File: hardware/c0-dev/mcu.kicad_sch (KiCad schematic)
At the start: 28 parts, among them J2 TAG_CONNECT, U11 W25Q128JVP, U12 RP2350A, Y1 ABM8-272-T3 (12Mhz)

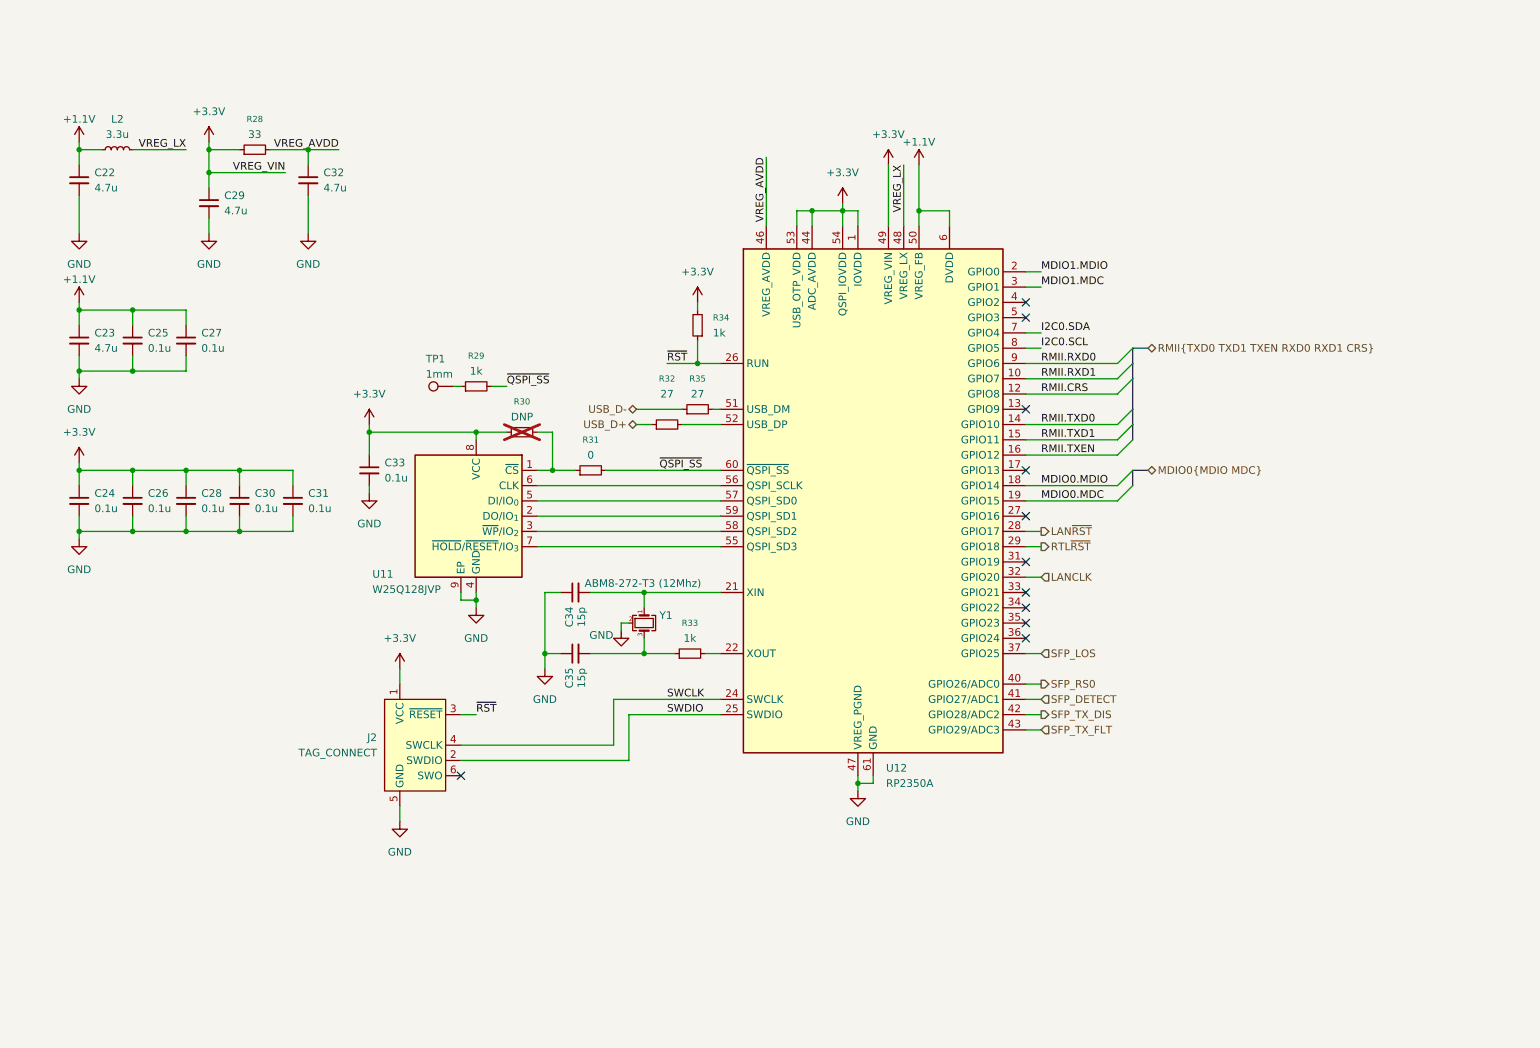
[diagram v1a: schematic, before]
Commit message: added 420 inputs
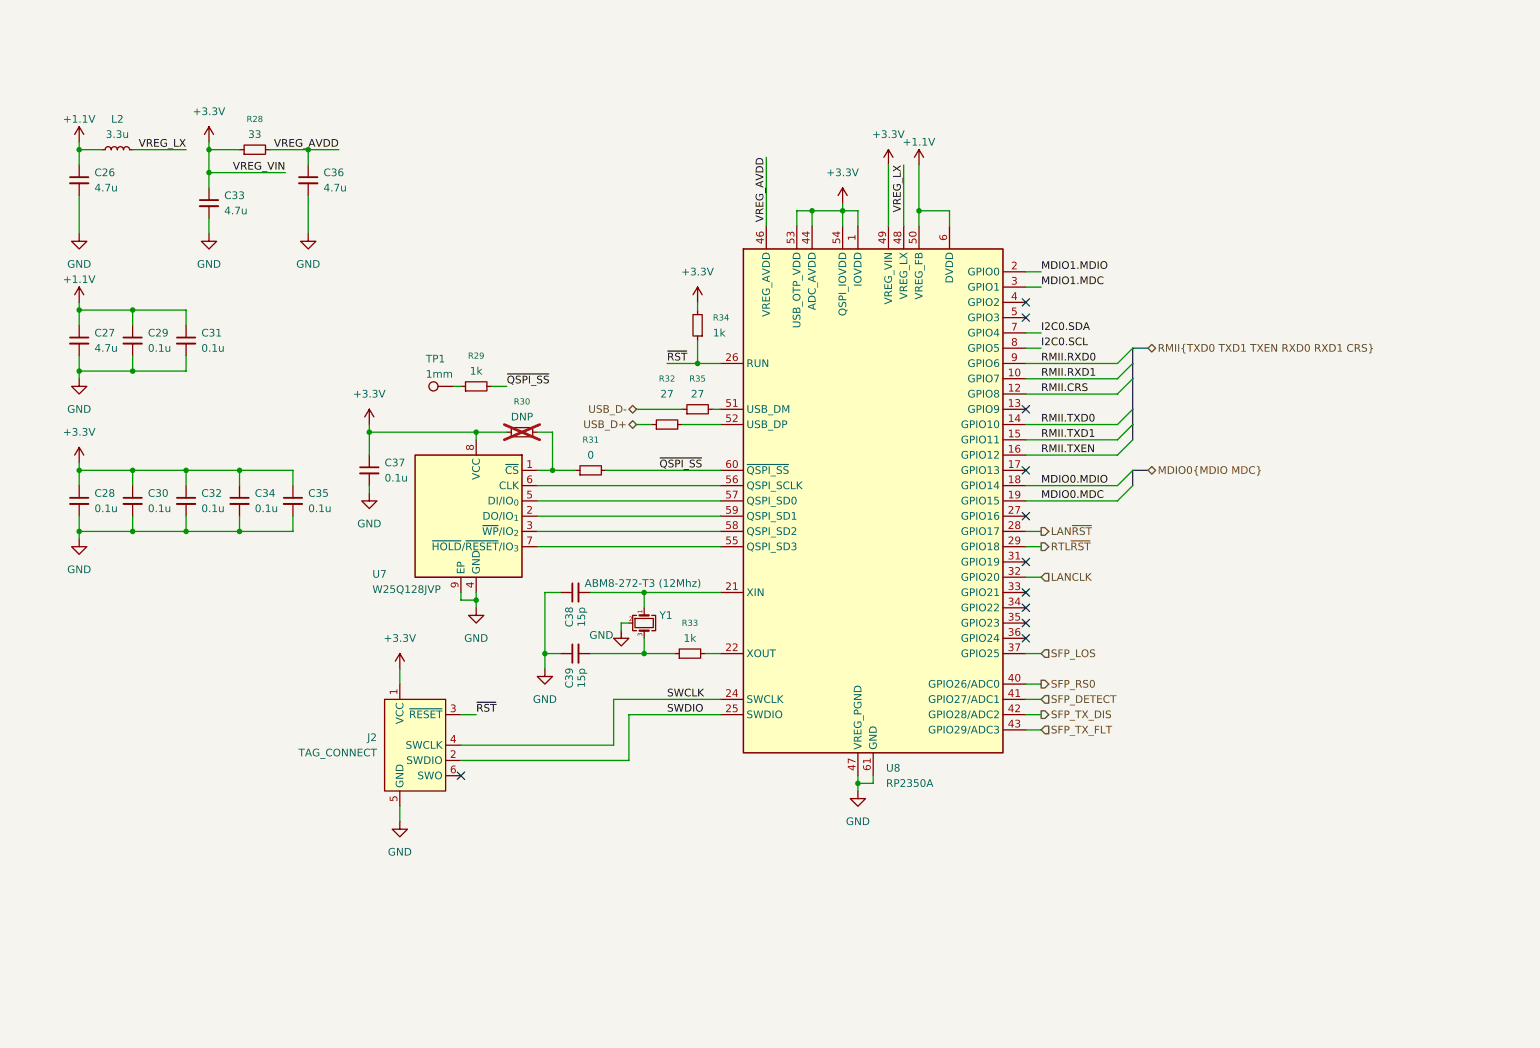
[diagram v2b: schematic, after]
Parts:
- renumbered C22 to C26, C23 to C27, C24 to C28, C25 to C29, C26 to C30, C27 to C31, C28 to C32, C29 to C33, C30 to C34, C31 to C35, C32 to C36, C33 to C37, C34 to C38, C35 to C39, U11 to U7, U12 to U8

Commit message: interface clanup and CAN
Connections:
- net I2C0.SCL: no longer names the net of U8.8 (GPIO5)
- net I2C0.SDA: no longer names the net of U8.7 (GPIO4)
- net LANCLK: no longer names the net of U8.32 (GPIO20)
- net MDIO1.MDC: no longer names the net of U8.3 (GPIO1)
- net MDIO1.MDIO: no longer names the net of U8.2 (GPIO0)
- net RTL~{RST}: no longer names the net of U8.29 (GPIO18)
- net SFP_DETECT: no longer names the net of U8.41 (GPIO27/ADC1)
- net SFP_LOS: no longer names the net of U8.37 (GPIO25)
- net SFP_RS0: no longer names the net of U8.40 (GPIO26/ADC0)
- net SFP_TX_DIS: no longer names the net of U8.42 (GPIO28/ADC2)
- net SFP_TX_FLT: no longer names the net of U8.43 (GPIO29/ADC3)
- no-connect marks 11 -> 22
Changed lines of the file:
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@@
+	)
+	(no_connect
+		(at 200.66 137.16)
 	)
 	(no_connect
@@
 	)
 	(no_connect
+		(at 200.66 127)
+	)
+	(no_connect
 		(at 200.66 111.76)
 	)
@@
 	)
 	(no_connect
+		(at 200.66 132.08)
+	)
+	(no_connect
 		(at 200.66 68.58)
 	)
@@
 	)
 	(no_connect
+		(at 200.66 66.04)
+	)
+	(no_connect
+		(at 200.66 114.3)
+	)
+	(no_connect
+		(at 200.66 73.66)
+	)
+	(no_connect
+		(at 200.66 76.2)
+	)
+	(no_connect
 		(at 106.68 147.32)
 	)
@@
 	)
 	(no_connect
+		(at 200.66 139.7)
+	)
+	(no_connect
+		(at 200.66 134.62)
+	)
+	(no_connect
 		(at 200.66 86.36)
 	)
@@
 	)
 	(no_connect
+		(at 200.66 63.5)
+	)
+	(no_connect
 		(at 200.66 96.52)
+	)
+	(no_connect
+		(at 200.66 109.22)
 	)
 	(bus_entry
@@
 	(wire
 		(pts
-			(xy 200.66 63.5) (xy 203.2 63.5)
-		)
-		(stroke
-			(width 0)
-			(type default)
-		)
-	)
-	(wire
-		(pts
 			(xy 187.96 53.34) (xy 182.88 53.34)
 		)
@@
 	(wire
 		(pts
-			(xy 200.66 139.7) (xy 203.2 139.7)
-		)
-		(stroke
-			(width 0)
-			(type default)
-		)
-	)
-	(wire
-		(pts
 			(xy 78.74 96.52) (xy 69.85 96.52)
 		)
@@
 	(wire
 		(pts
-			(xy 200.66 114.3) (xy 203.2 114.3)
-		)
-		(stroke
-			(width 0)
-			(type default)
-		)
-	)
-	(wire
-		(pts
 			(xy 52.07 43.18) (xy 60.96 43.18)
 		)
@@
 	(wire
 		(pts
-			(xy 200.66 127) (xy 203.2 127)
-		)
-		(stroke
-			(width 0)
-			(type default)
-		)
-	)
-	(wire
-		(pts
 			(xy 64.77 46.99) (xy 64.77 49.53)
 		)
@@
 	(wire
 		(pts
-			(xy 203.2 73.66) (xy 200.66 73.66)
-		)
-		(stroke
-			(width 0)
-			(type default)
-		)
-	)
-	(wire
-		(pts
 			(xy 60.96 104.14) (xy 60.96 106.68)
 		)
@@
 	(wire
 		(pts
-			(xy 203.2 76.2) (xy 200.66 76.2)
-		)
-		(stroke
-			(width 0)
-			(type default)
-		)
-	)
-	(wire
-		(pts
 			(xy 78.74 104.14) (xy 78.74 106.68)
 		)
@@
 	(wire
 		(pts
-			(xy 200.66 137.16) (xy 203.2 137.16)
-		)
-		(stroke
-			(width 0)
-			(type default)
-		)
-	)
-	(wire
-		(pts
 			(xy 172.72 148.59) (xy 172.72 149.86)
 		)
@@
 	(wire
 		(pts
-			(xy 200.66 109.22) (xy 203.2 109.22)
-		)
-		(stroke
-			(width 0)
-			(type default)
-		)
-	)
-	(wire
-		(pts
 			(xy 52.07 96.52) (xy 43.18 96.52)
 		)
@@
 	(wire
 		(pts
-			(xy 200.66 66.04) (xy 203.2 66.04)
-		)
-		(stroke
-			(width 0)
-			(type default)
-		)
-	)
-	(wire
-		(pts
 			(xy 119.38 106.68) (xy 149.86 106.68)
 		)
@@
 	(wire
 		(pts
-			(xy 200.66 134.62) (xy 203.2 134.62)
-		)
-		(stroke
-			(width 0)
-			(type default)
-		)
-	)
-	(wire
-		(pts
 			(xy 106.68 144.78) (xy 134.62 144.78)
 		)
@@
 		(pts
 			(xy 64.77 41.91) (xy 64.77 43.18)
-		)
-		(stroke
-			(width 0)
-			(type default)
-		)
-	)
-	(wire
-		(pts
-			(xy 200.66 132.08) (xy 203.2 132.08)
 		)
 		(stroke
@@
 		)
 	)
-	(label "I2C0.SDA"
-		(at 203.2 73.66 0)
-		(effects
-			(font
-				(size 1.27 1.27)
-			)
-			(justify left bottom)
-		)
-	)
 	(label "~{RST}"
 		(at 109.22 137.16 0)
@@
 		)
 	)
-	(label "MDIO1.MDIO"
-		(at 203.2 63.5 0)
-		(effects
-			(font
-				(size 1.27 1.27)
-			)
-			(justify left bottom)
-		)
-	)
 	(label "~{RST}"
 		(at 140.97 78.74 0)
@@
 	(label "SWCLK"
 		(at 140.97 134.62 0)
-		(effects
-			(font
-				(size 1.27 1.27)
-			)
-			(justify left bottom)
-		)
-	)
-	(label "MDIO1.MDC"
-		(at 203.2 66.04 0)
-		(effects
-			(font
-				(size 1.27 1.27)
-			)
-			(justify left bottom)
-		)
-	)
-	(label "I2C0.SCL"
-		(at 203.2 76.2 0)
 		(effects
 			(font
@@
 		)
 	)
-	(hierarchical_label "SFP_LOS"
-		(shape input)
-		(at 203.2 127 0)
-		(effects
-			(font
-				(size 1.27 1.27)
-			)
-			(justify left)
-		)
-	)
-	(hierarchical_label "LANCLK"
-		(shape input)
-		(at 203.2 114.3 0)
-		(effects
-			(font
-				(size 1.27 1.27)
-			)
-			(justify left)
-		)
-	)
-	(hierarchical_label "SFP_RS0"
-		(shape output)
-		(at 203.2 132.08 0)
-		(effects
-			(font
-				(size 1.27 1.27)
-			)
-			(justify left)
-		)
-	)
-	(hierarchical_label "RTL~{RST}"
-		(shape output)
-		(at 203.2 109.22 0)
-		(effects
-			(font
-				(size 1.27 1.27)
-			)
-			(justify left)
-		)
-	)
 	(hierarchical_label "USB_D-"
 		(shape bidirectional)
@@
 		)
 	)
-	(hierarchical_label "SFP_TX_FLT"
-		(shape input)
-		(at 203.2 139.7 0)
-		(effects
-			(font
-				(size 1.27 1.27)
-			)
-			(justify left)
-		)
-	)
 	(hierarchical_label "LAN~{RST}"
 		(shape output)
@@
 		)
 	)
-	(hierarchical_label "SFP_DETECT"
-		(shape input)
-		(at 203.2 134.62 0)
-		(effects
-			(font
-				(size 1.27 1.27)
-			)
-			(justify left)
-		)
-	)
 	(hierarchical_label "RMII{TXD0 TXD1 TXEN RXD0 RXD1 CRS}"
 		(shape bidirectional)
@@
 		(effects
 			(font
-				(size 1.27 1.27)
-			)
-			(justify left)
-		)
-	)
-	(hierarchical_label "SFP_TX_DIS"
-		(shape output)
-		(at 203.2 137.16 0)
-		(effects
-			(font

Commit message: i2c address check
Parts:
- renumbered R28 to R29, R29 to R30, R30 to R31, R31 to R32, R32 to R33, R33 to R34, R34 to R35, R35 to R36
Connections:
- net USB_D+: now also R36.1; no longer R33.1
- net USB_D-: now also R33.1; no longer R36.1
- net LAN_CLK: now reaches U8.33 (GPIO21)
- net POE_T2P: now reaches U8.43 (GPIO29/ADC3)
- no-connect marks 22 -> 20
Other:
- moved on the sheet: C37, C38, C39, J2, R30, R31, R32, R33, R34, R35, R36, TP1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

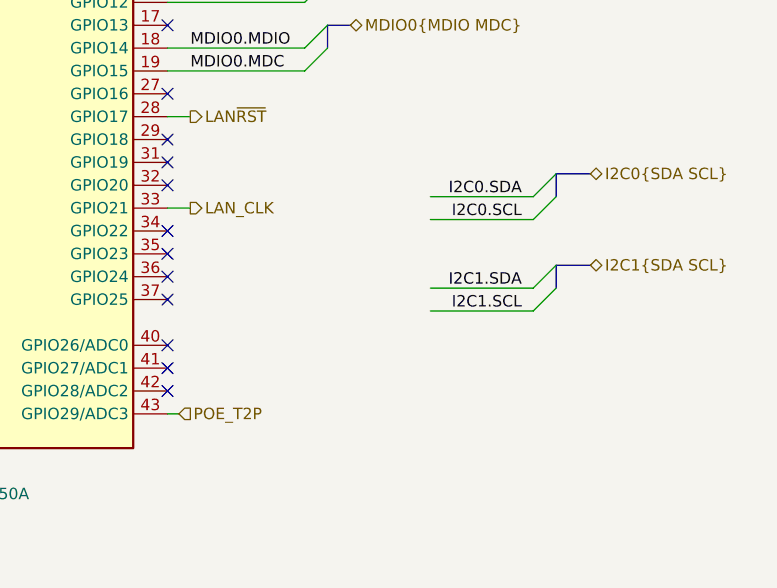
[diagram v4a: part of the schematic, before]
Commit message: introduced MCU isolation netclass
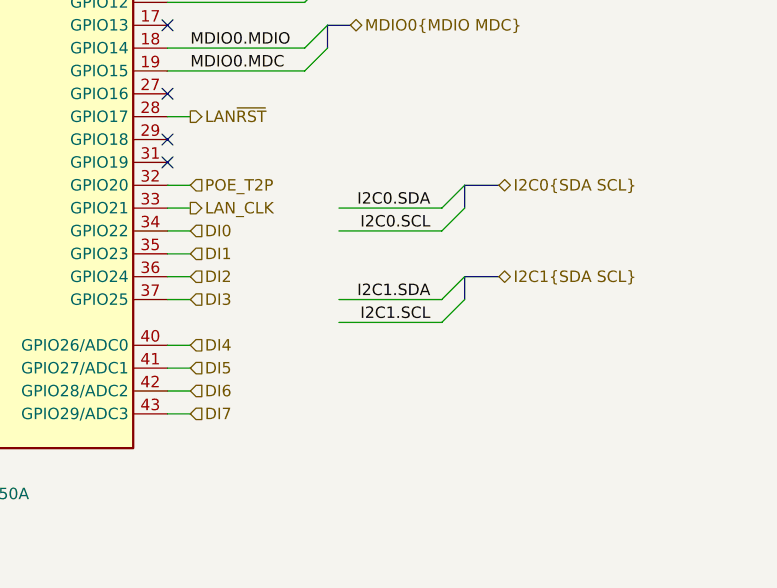
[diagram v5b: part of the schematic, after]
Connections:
- net POE_T2P: now also U8.32 (GPIO20); no longer U8.43 (GPIO29/ADC3)
- net DI0: now reaches U8.34 (GPIO22)
- net DI1: now reaches U8.35 (GPIO23)
- net DI2: now reaches U8.36 (GPIO24)
- net DI3: now reaches U8.37 (GPIO25)
- net DI4: now reaches U8.40 (GPIO26/ADC0)
- net DI5: now reaches U8.41 (GPIO27/ADC1)
- net DI6: now reaches U8.42 (GPIO28/ADC2)
- new net DI7: U8.43 (GPIO29/ADC3)
- no-connect marks 20 -> 12
